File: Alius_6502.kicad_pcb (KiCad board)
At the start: 2 copper layers, 208 x 175 mm, 120 parts, among them J1 Conn_01x02_Male, J2 I/O, J3 Power, J4 SD_Card, J5 Conn_01x02_Male, SW1 SW_Push, U10 74HC595, U11 74HC595, U12 74HC595, U13 74HC595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

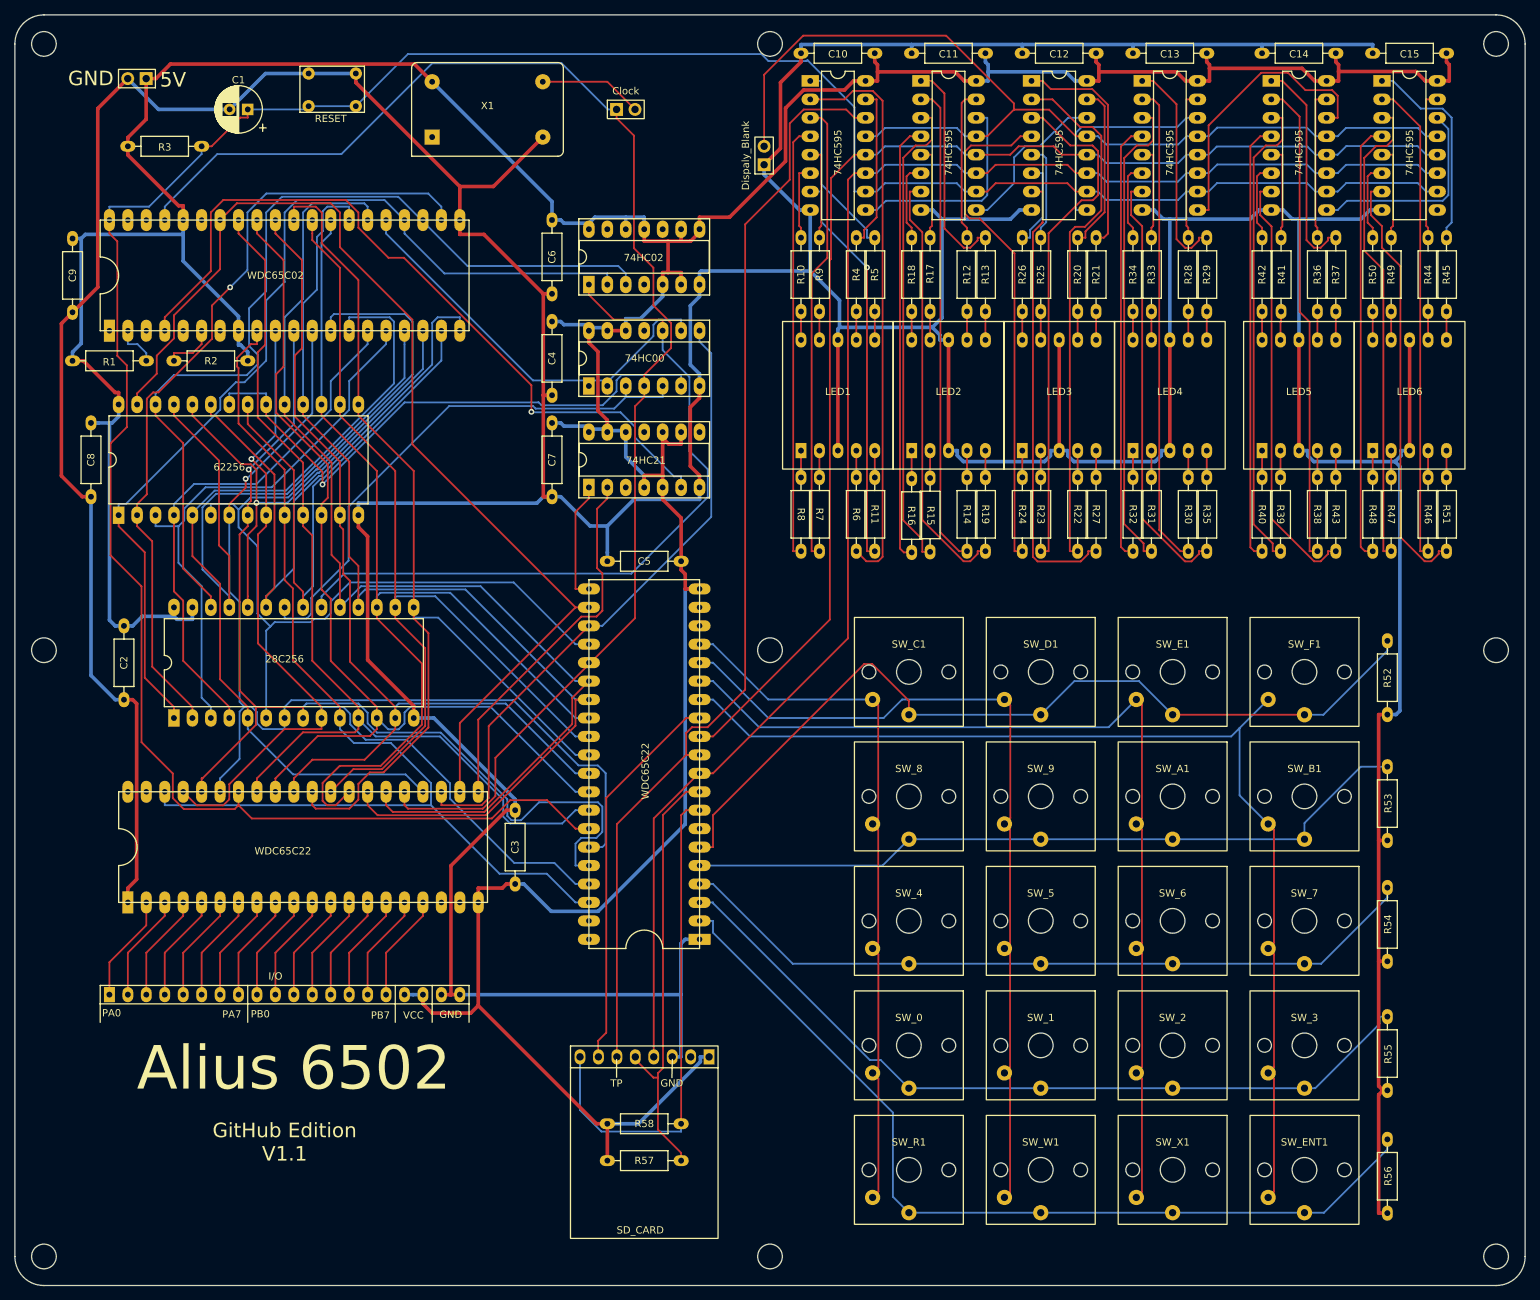
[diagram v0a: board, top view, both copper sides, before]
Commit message: Tidy up of track routing to give more clearance. Tidy up missing silkscreen of chip numbers.
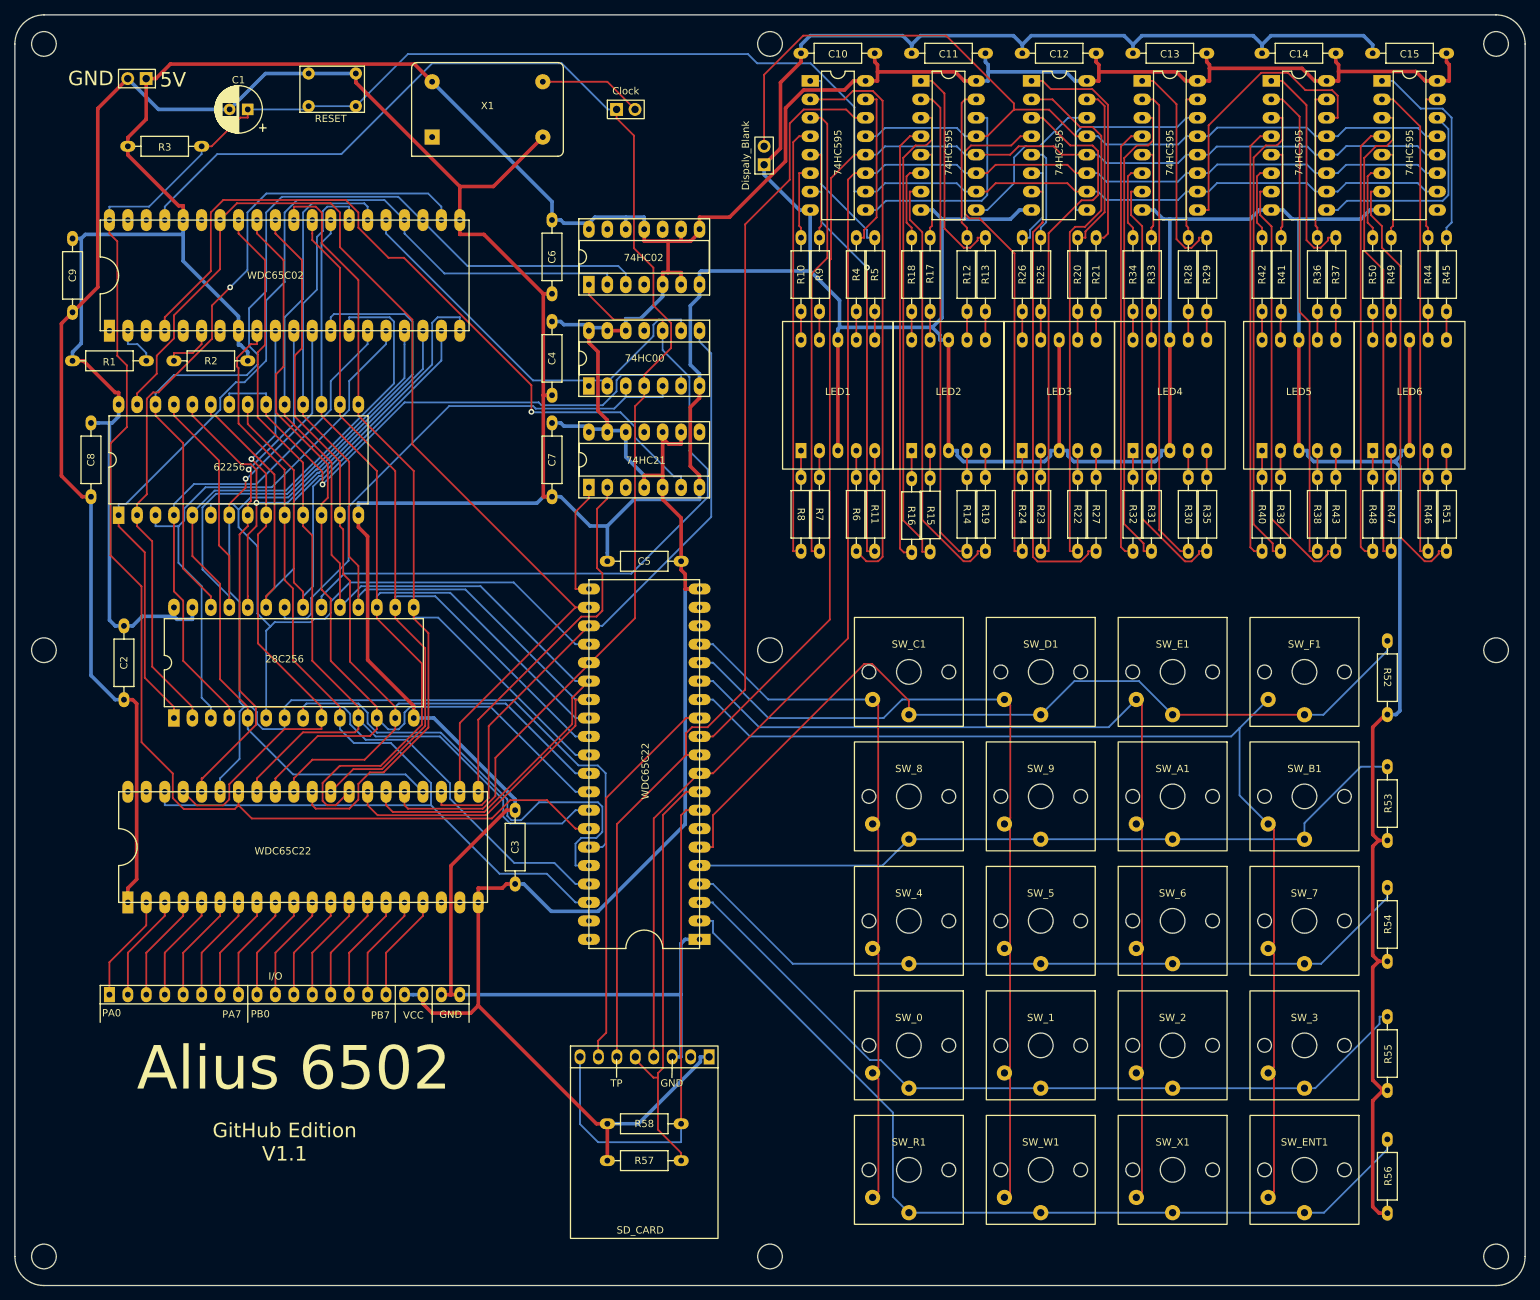
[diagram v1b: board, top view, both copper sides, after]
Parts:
- turned R52 to -90 degrees
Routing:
- net GND: track 991.0 -> 998.1 mm
- net SD_Detect: track 68.9 -> 72.1 mm

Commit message: Version 1.2
Improved reset.
Added connection for PWM display brightness.

NOTE: This board revision is yet to be made and tested.
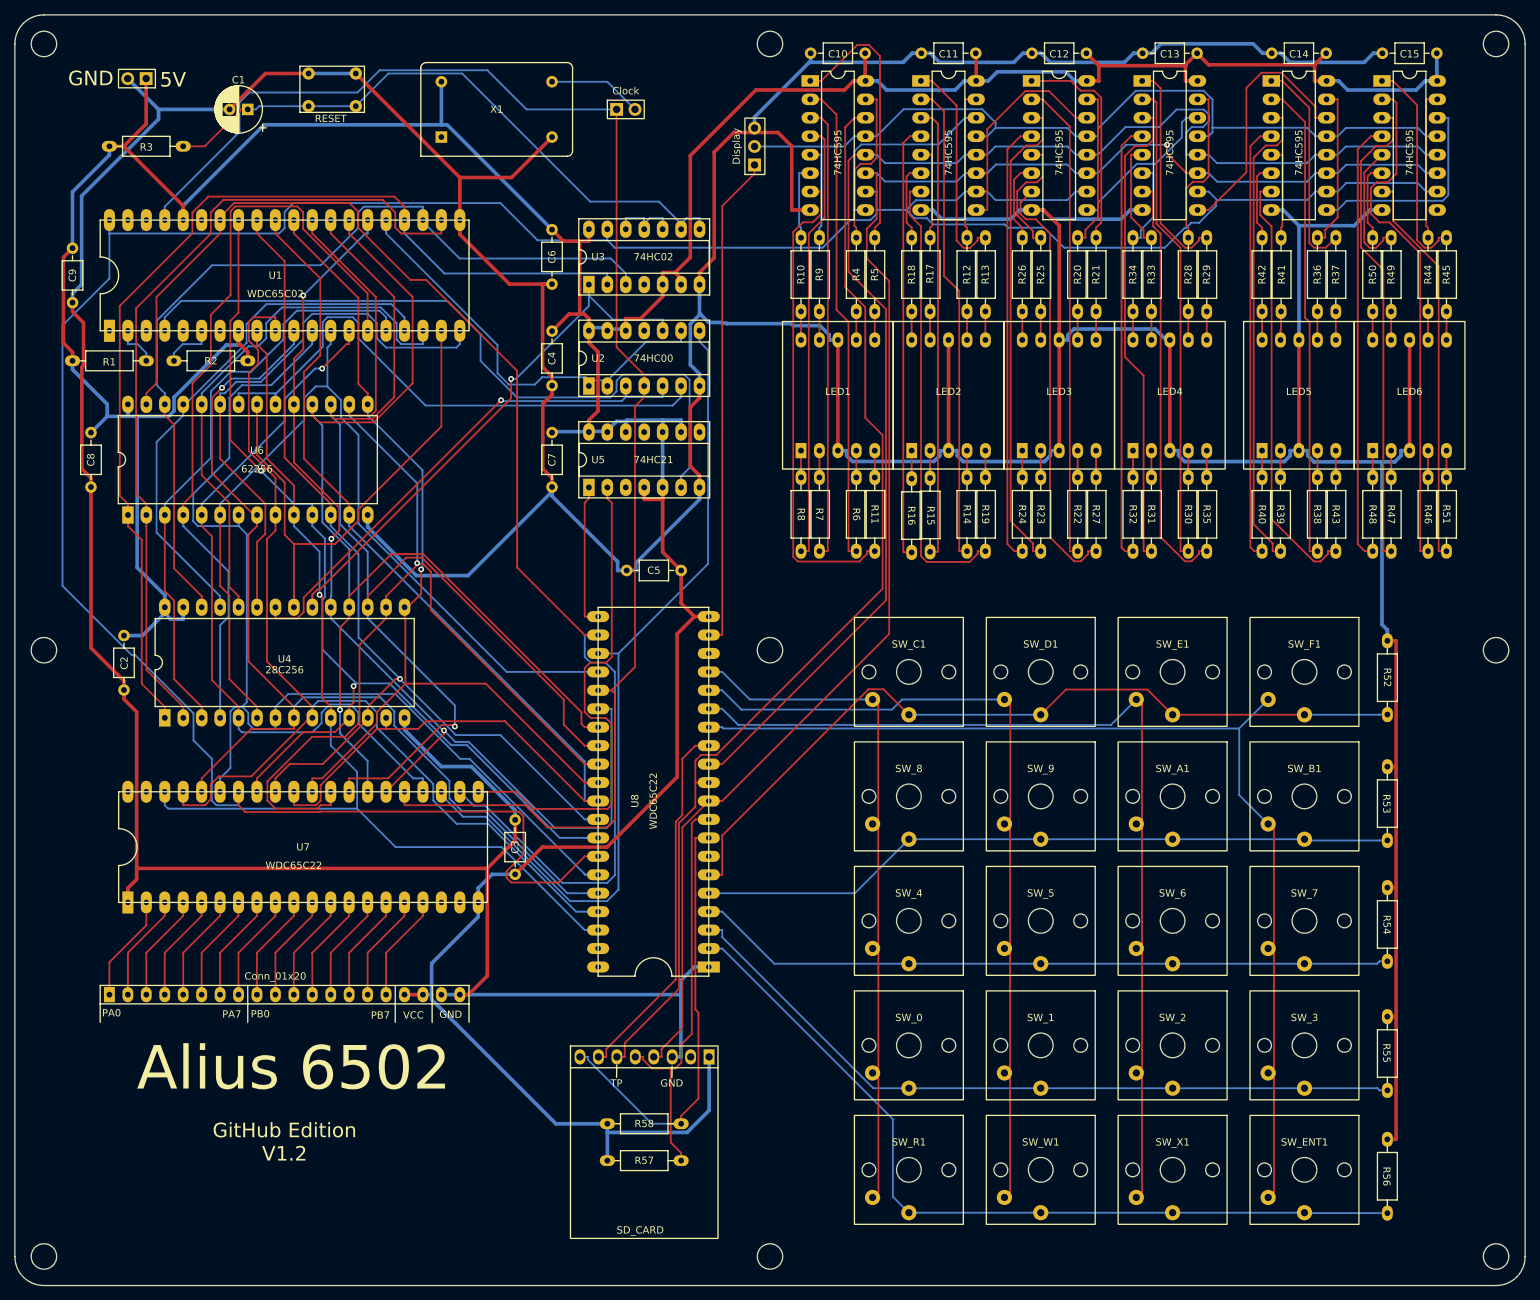
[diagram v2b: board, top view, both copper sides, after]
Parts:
- removed J5: Conn_01x02_Male, Alius_6502:2_pin_header
- added Display: ~, Alius_6502:3_pin_header, F.Cu at (121.9, 40.7)
- added HOLE1: MountingHole_3.5mm, MountingHole:MountingHole_3.5mm, F.Cu at (24.0, 24.0)
- added HOLE2: MountingHole_3.5mm, MountingHole:MountingHole_3.5mm, F.Cu at (124.0, 24.0)
- added HOLE4: MountingHole_3.5mm, MountingHole:MountingHole_3.5mm, F.Cu at (24.0, 107.5)
- added HOLE5: MountingHole_3.5mm, MountingHole:MountingHole_3.5mm, F.Cu at (124.0, 107.5)
- added HOLE6: MountingHole_3.5mm, MountingHole:MountingHole_3.5mm, F.Cu at (224.0, 107.5)
- added HOLE7: MountingHole_3.5mm, MountingHole:MountingHole_3.5mm, F.Cu at (24.0, 191.0)
- added HOLE8: MountingHole_3.5mm, MountingHole:MountingHole_3.5mm, F.Cu at (124.0, 191.0)
- added HOLE9: MountingHole_3.5mm, MountingHole:MountingHole_3.5mm, F.Cu at (224.0, 191.0)
- added Hole3: MountingHole_3.5mm, MountingHole:MountingHole_3.5mm, F.Cu at (224.0, 24.0)
- C10, C11, C12, C13, C14, C15, C2, C3, C4, C5, C6, C7, C8, C9: footprint Alius_6502:R_Axial_DIN0207_L6.3mm_D2.5mm_P10.16mm_Horizontal -> Alius_6502:C_Axial_L3.8mm_D2.6mm_P7.50mm_Horizontal
- J2: value I/O -> Conn_01x20
- LED1, LED2, LED3, LED4, LED5, LED6: value 7-seg -> 7-SEG-SC56-11
- U4: renamed from 28C256; footprint Alius_6502:DIP-28_W15.24mm_LongPads -> Alius_6502:28-pin-DIP
- U6: footprint Alius_6502:DIP-28_W15.24mm_LongPads -> Alius_6502:28-pin-DIP
- X1: footprint Alius_6502:Oscillator_DIP-14 -> Oscillator:Oscillator_DIP-14
- moved X1 7.41 mm to (78.7, 36.8)
- moved U8 4.02 mm to (108.0, 128.3)
- moved R3 2.54 mm to (38.1, 38.1)
- moved U6 2.54 mm to (52.1, 81.3)
- moved C5 1.84 mm to (108.0, 96.5)
- turned R53 to -90 degrees
- turned R54 to -90 degrees
- turned R55 to -90 degrees
- turned R56 to -90 degrees
- renumbered WDC65C02 to U1, 74HC00 to U2, 74HC02 to U3, 74HC21 to U5
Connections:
- C1 pad 1: RESET -> RESET_BTN
- R3 pad 2: RESET -> RESET_BTN
- SW1 pad 2: RESET -> RESET_BTN
- U10 pad 12: 7seg_CS -> 7Seg_CS
- U11 pad 12: 7seg_CS -> 7Seg_CS
- U12 pad 12: 7seg_CS -> 7Seg_CS
- U13 pad 12: 7seg_CS -> 7Seg_CS
- U14 pad 12: 7seg_CS -> 7Seg_CS
- U3 pad 10: unconnected-(U3-Pad10) -> Net-(U3-3Y)
- U3 pad 11: VCC -> Net-(U3-3Y)
- U3 pad 12: VCC -> Net-(U3-3Y)
- U3 pad 13: unconnected-(U3-Pad13) -> RESET
- U3 pad 8: VCC -> RESET_BTN
- U3 pad 9: VCC -> RESET_BTN
- U8 pad 19: unconnected-(U8-Pad19) -> DisplayPWM
- U9 pad 12: 7seg_CS -> 7Seg_CS
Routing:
- net RESET_BTN: track 0.00 -> 86.6 mm
- net DisplayPWM: track 0.00 -> 68.4 mm
- net RW: track 149.8 -> 189.5 mm
- net /A6: track 72.6 -> 106.1 mm
- net RESET: track 362.7 -> 396.1 mm
- net IO_CS: track 87.6 -> 116.9 mm
- net /D2: track 128.8 -> 157.3 mm
- net /D4: track 129.1 -> 155.7 mm, vias 0 -> 1
- net ROM_CS: track 100.4 -> 73.8 mm, vias 0 -> 1
- net 7seg_OE: track 136.8 -> 113.2 mm
- net /D5: track 138.0 -> 158.9 mm, vias 0 -> 1
- net 7Seg_CS: track 175.1 -> 195.3 mm
- net IRQ_B: track 51.1 -> 69.2 mm
- net GND: track 998.1 -> 1014.7 mm
- net /A4: track 139.9 -> 124.8 mm
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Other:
- outline, holes or cut-outs redrawn
- board text added: "GitHub Edition V1.2"
- board text removed: "GitHub Edition V1.1"

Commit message: Version 1.2
Improved reset circuit.
Support for software brightness.
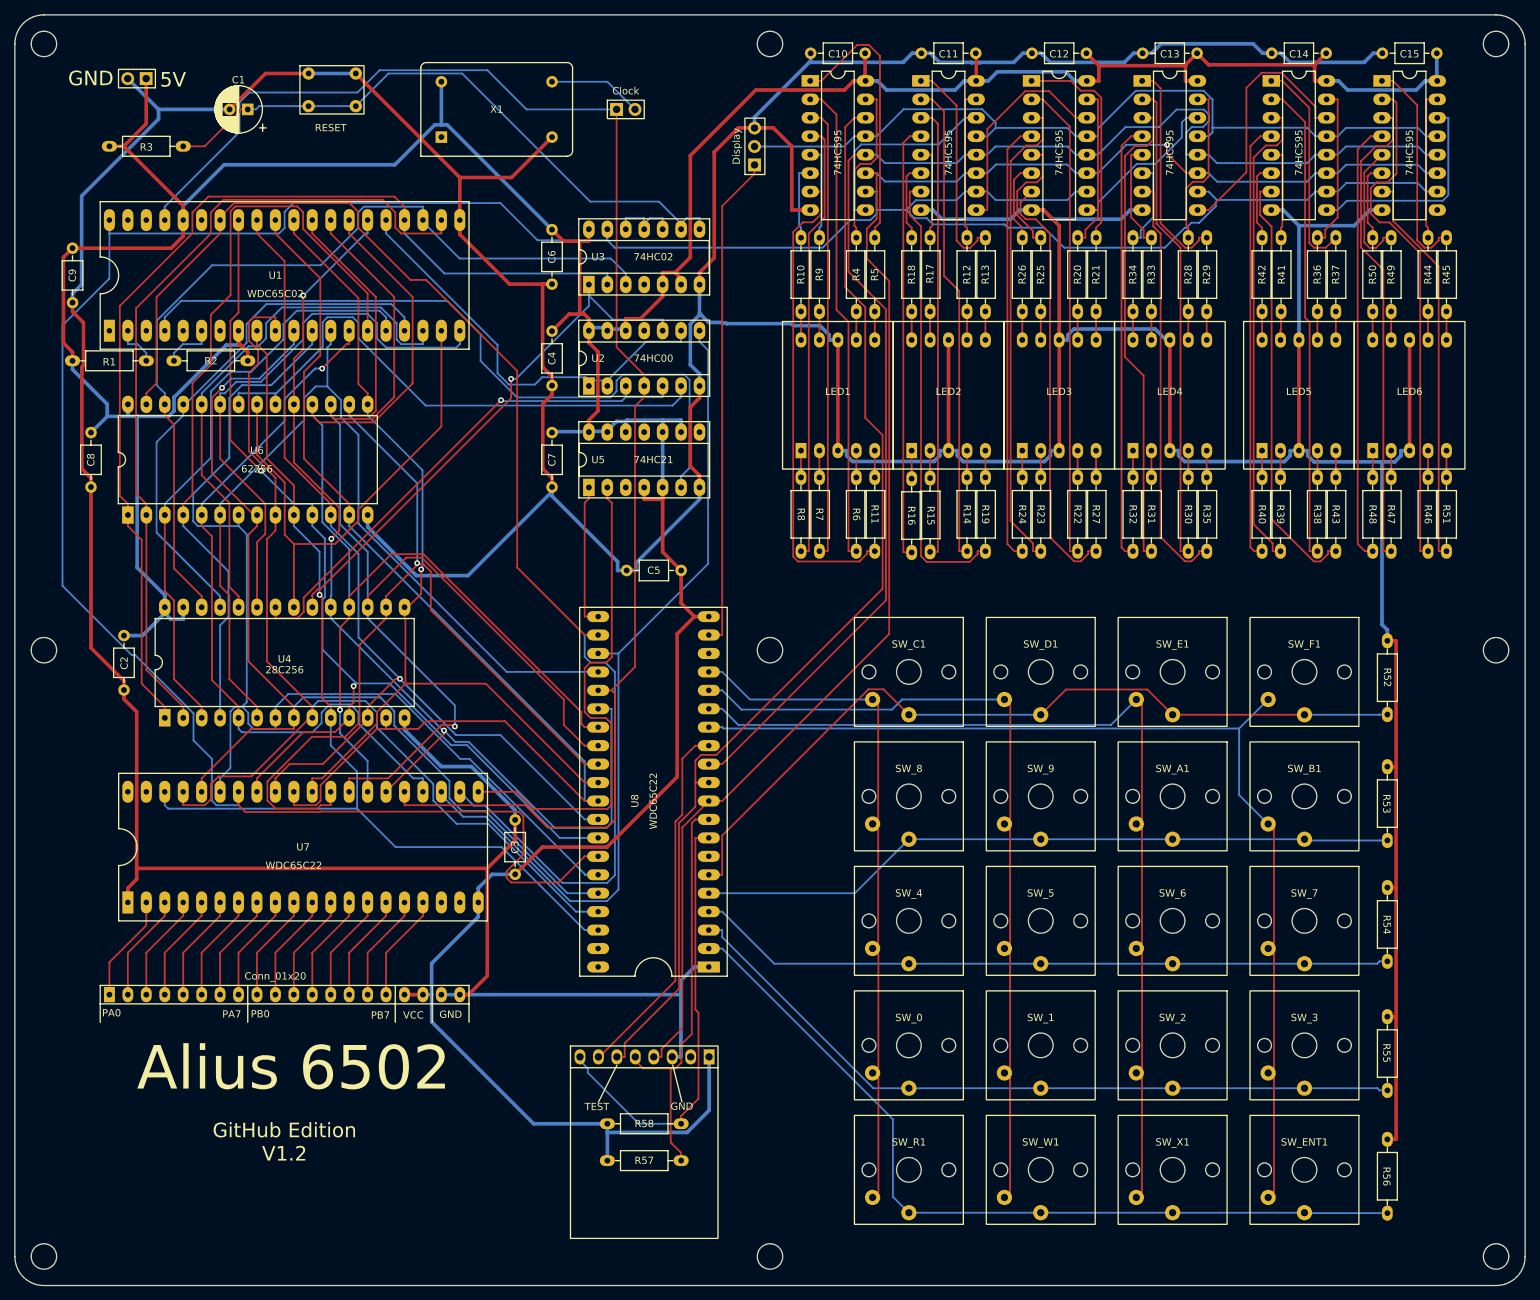
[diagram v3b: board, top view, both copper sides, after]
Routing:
- net VCC: track 622.1 -> 625.9 mm
- net GND: track 1014.7 -> 1015.5 mm
- net SD_Card_CS: track 50.9 -> 50.3 mm
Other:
- board text removed: "SD_CARD"
- board text removed: "TP"
